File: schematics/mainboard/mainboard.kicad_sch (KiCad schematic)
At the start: 50 parts

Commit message: SCH: maionboard base, routing in progress
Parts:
- removed C10, C11, C12, C13, C14, C15, C16, C17, C18, C19, C5, C6, C7, C8, C9: ~, symbol Arduino_MEGA_2560-Rev3:SMARTPRJ_C-EU0603-RND
- removed D1: ~, symbol Arduino_MEGA_2560-Rev3:DIODE_DIODE-SMB
- removed D2, D3: ~, symbol Arduino_MEGA_2560-Rev3:DIODE_DIODE-MINIMELF
- removed F1: ~, symbol Arduino_MEGA_2560-Rev3:RCL_L-EUL1812
- removed GROUND1, RESET-EN1: ~, symbol Arduino_MEGA_2560-Rev3:JUMPER_SJ
- removed IC1: ~, symbol Arduino_MEGA_2560-Rev3:LINEAR_MC33269ST-3.3T3
- removed IC2: ~, symbol Arduino_MEGA_2560-Rev3:LINEAR_LMV358MMX
- removed IC3: ~, symbol Arduino_MEGA_2560-Rev3:SMARTPRJ_ATMEGA25602560-16AU
- removed IC4: ~, symbol Arduino_MEGA_2560-Rev3:SMARTPRJ_LP2985-XXDBVR33
- removed IC5: ~, symbol Arduino_MEGA_2560-Rev3:SMARTPRJ_ATMEGA16U2-MU
- removed ICSP1_1, ICSP_1: ~, symbol Arduino_MEGA_2560-Rev3:SMARTPRJ_PINHD-2X3
- removed JP3: ~, symbol Arduino_MEGA_2560-Rev3:SMARTPRJ_PINHD-2X2
- removed L2: ~, symbol Arduino_MEGA_2560-Rev3:WUERTH-ELEKTRONIK_WE-CBF_0805
- removed PC1, PC2: ~, symbol Arduino_MEGA_2560-Rev3:RCL_CPOL-EUD
- removed POWER1: ~, symbol Arduino_MEGA_2560-Rev3:SMARTPRJ_PINHD-1X8
- removed R3, R4: ~, symbol Arduino_MEGA_2560-Rev3:SMARTPRJ_R-EU_R0603
- removed RESET1: ~, symbol Arduino_MEGA_2560-Rev3:SMARTPRJ_TS42
- removed RN1, RN4: ~, symbol Arduino_MEGA_2560-Rev3:RESISTOR-DIL_4R-NCAT16
- removed RN2, RN3, RN5: ~, symbol Arduino_MEGA_2560-Rev3:RESISTOR-DIL_4R-NCAY16
- removed RX1, TX1: ~, symbol Arduino_MEGA_2560-Rev3:LED_LEDCHIP-LED0805
- removed T1: ~, symbol Arduino_MEGA_2560-Rev3:ZETEX_PMOSSOT23
- removed X1: ~, symbol Arduino_MEGA_2560-Rev3:SMARTPRJ_POWERSUPPLY_DC21MMX
- removed X2: ~, symbol Arduino_MEGA_2560-Rev3:SMARTPRJ_PN61729
- removed Y1: ~, symbol Arduino_MEGA_2560-Rev3:SMARTPRJ_RESONATORMU
- removed Y2: ~, symbol Arduino_MEGA_2560-Rev3:SMARTPRJ_XTAL_S
- removed Z1, Z2: ~, symbol Arduino_MEGA_2560-Rev3:VARISTOR_VARISTORCN0603
- added C1, C2, C3, C4, C5, C6: 0.1uF, Capacitor_SMD:C_0603_1608Metric, symbol Device:C
- added C7, C8: 22pF, Capacitor_SMD:C_0603_1608Metric, symbol Device:C_Small
- added D1, D2: LED, LED_SMD:LED_1206_3216Metric, symbol Device:LED
- added J1: ICSP, Connector_PinHeader_2.54mm:PinHeader_2x03_P2.54mm_Vertical, symbol Connector_Generic:Conn_02x03_Odd_Even
- added J2: USB_B_Micro, Connector_USB:USB_Micro-B_GCT_USB3076-30-A, symbol Connector:USB_B_Micro
- added J3: Jack-DC, Connector_BarrelJack:BarrelJack_CLIFF_FC681465S_SMT_Horizontal, symbol Connector:Jack-DC
- added J4: PWR_SELECT, Connector_PinHeader_2.54mm:PinHeader_1x03_P2.54mm_Vertical, symbol Connector:Conn_01x03_Pin
- added R1, R2, R4, R5: 1k, Resistor_SMD:R_0603_1608Metric, symbol Device:R
- added R3: 10K, Resistor_SMD:R_0603_1608Metric, symbol Device:R
- added U1: ATmega2560-16A, Package_QFP:TQFP-100_14x14mm_P0.5mm, symbol MCU_Microchip_ATmega:ATmega2560-16A
- added U2: FT232RL, Package_SO:SSOP-28_5.3x10.2mm_P0.65mm, symbol Interface_USB:FT232RL
- added Y1: 16Mhz, Crystal:Crystal_HC52-8mm_Vertical, symbol Device:Crystal
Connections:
- net +5V: now also C1.1, C2.1, C3.1, C4.1, J1.2 (Pin_2), J4.2 (Pin_2), R3.1, R4.2, R5.2, U1.10 (VCC), U1.100 (AVCC), U1.31 (VCC), U1.61 (VCC), U1.80 (VCC), U2.19 (~{RESET}), U2.20 (VCC), U2.4 (VCCIO)
- net DTR: now also C6.2, U2.2 (DTR)
- net GND: now also C1.2, C2.2, C3.2, C4.2, C5.2, C7.2, C8.2, J1.6 (Pin_6), J2.5 (GND), J2.6 (Shield), J3.2, U1.11 (GND), U1.32 (GND), U1.62 (GND), U1.81 (GND), U1.99 (GND), U2.18 (GND), U2.21 (GND), U2.25 (AGND), U2.7 (GND)
- net RESET: now also C5.1, C6.1, J1.5 (Pin_5), R3.2, U1.30 (~{RESET})
- new net: R1.1, U2.1 (TXD)
- new net: R1.2, U1.2 (PE0)
- new net: C7.1, U1.34 (XTAL1), Y1.1
- new net: C8.1, U1.33 (XTAL2), Y1.2
- new net: J2.1 (VBUS), J4.3 (Pin_3)
- new net: J2.2 (D-), U2.16 (USBD-)
- new net: J2.3 (D+), U2.15 (USBD+)
- new net: R2.1, U2.5 (RXD)
- new net: R2.2, U1.3 (PE1)
- new net: J3.1, J4.1 (Pin_1)
- new net: D2.1 (K), U2.22 (CBUS1)
- new net: D2.2 (A), R5.1
- new net: D1.1 (K), U2.23 (CBUS0)
- new net: D1.2 (A), R4.1
- new net MISO: J1.1 (Pin_1), U1.22 (PB3)
- new net MOSI: J1.4 (Pin_4), U1.21 (PB2)
- new net SCK: J1.3 (Pin_3), U1.20 (PB1)
- no-connect marks 81 -> 9
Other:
- note added: "Programming header"
- note removed: "(MISO)"
- note removed: "(MOSI)"
- note removed: "(RX0)"
- note removed: "(SCK)"
- note removed: "(TX0)"
- note removed: "USB boot En"

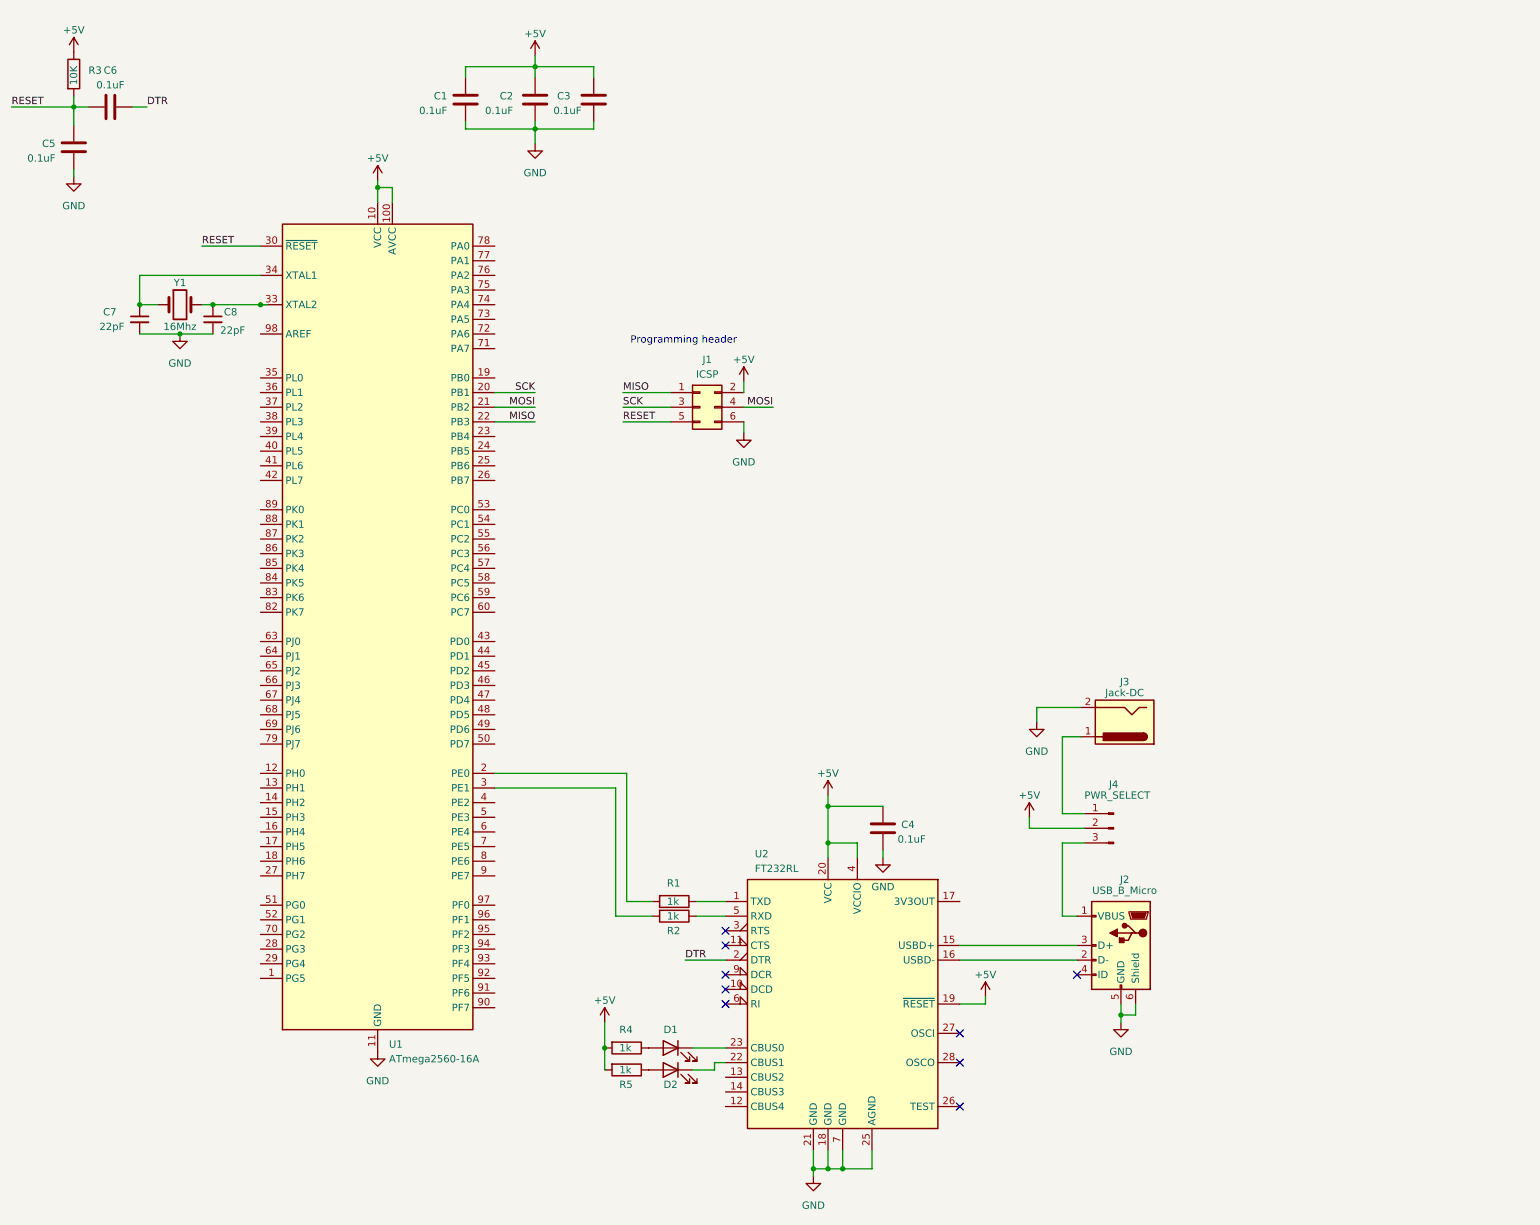
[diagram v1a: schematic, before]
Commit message: SCH: mainboard: cont.
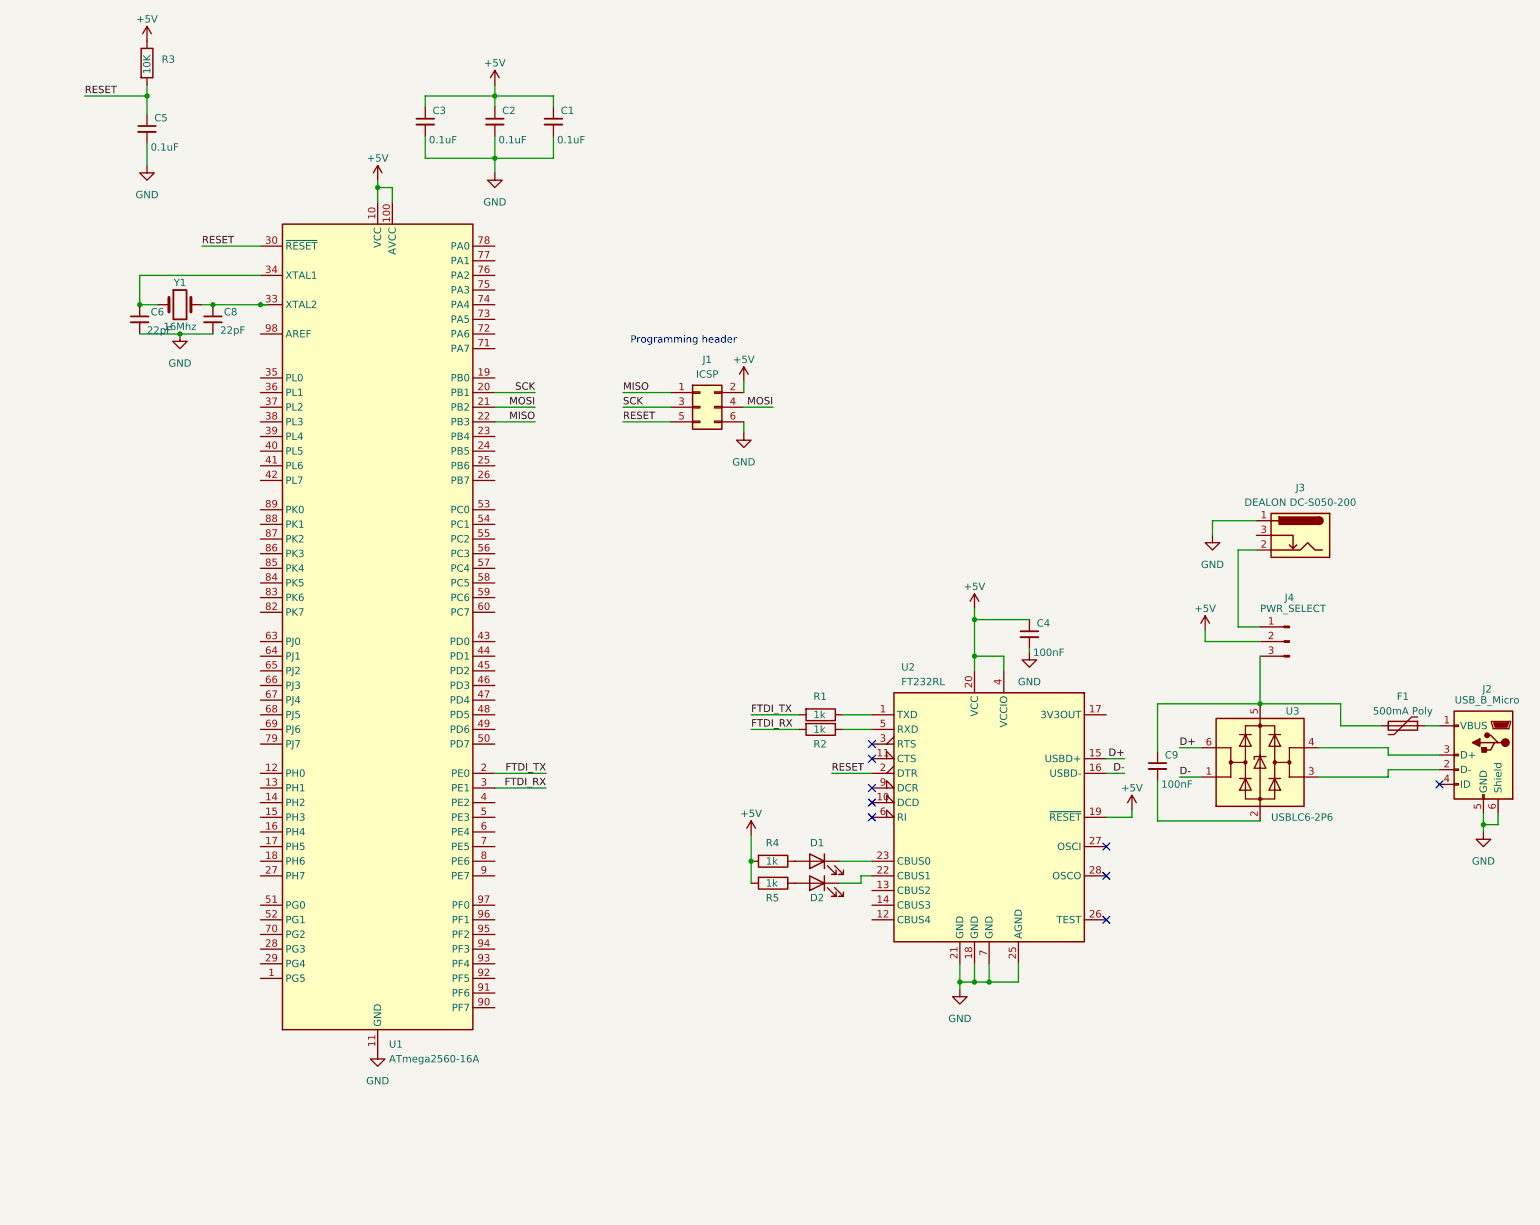
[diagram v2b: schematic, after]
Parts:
- removed C1, C2, C3, C4, C5, C6: 0.1uF, Capacitor_SMD:C_0603_1608Metric, symbol Device:C
- removed C7: 22pF, Capacitor_SMD:C_0603_1608Metric, symbol Device:C_Small
- removed J3: Jack-DC, Connector_BarrelJack:BarrelJack_CLIFF_FC681465S_SMT_Horizontal, symbol Connector:Jack-DC
- added C1, C2, C3, C5: 0.1uF, Capacitor_SMD:C_0201_0603Metric, symbol Device:C_Small
- added C4, C9: 100nF, Capacitor_SMD:C_0201_0603Metric, symbol Device:C_Small
- added C6: 22pF, Capacitor_SMD:C_0603_1608Metric, symbol Device:C_Small
- added F1: 500mA Poly, Fuse:Fuse_0603_1608Metric, symbol Device:Polyfuse
- added J3: DEALON DC-S050-200, Connector_BarrelJack:BarrelJack_CLIFF_FC681465S_SMT_Horizontal, symbol Connector:Barrel_Jack_Switch
- added U3: USBLC6-2P6, Package_TO_SOT_SMD:SOT-666, symbol Power_Protection:USBLC6-2P6
- C8: lcsc (none) -> C105620
- J2: footprint Connector_USB:USB_Micro-B_GCT_USB3076-30-A -> Connector_USB:USB_Micro-B_Molex-105017-0001; lcsc (none) -> C962222
- R1, R2, R4, R5: lcsc (none) -> C21190
- R3: lcsc (none) -> C25804
- U1: lcsc (none) -> C22460
- U2: footprint Package_SO:SSOP-28_5.3x10.2mm_P0.65mm -> Package_DFN_QFN:HVQFN-32-1EP_5x5mm_P0.5mm_EP3.1x3.1mm
- Y1: footprint Crystal:Crystal_HC52-8mm_Vertical -> Crystal:Crystal_SMD_5032-2Pin_5.0x3.2mm; lcsc (none) -> C112572
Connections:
- net DTR is gone; now on net RESET: U2.2 (DTR)
- net +5V: now also C1.1, C2.1, C3.1, C4.1
- net GND: now also C1.2, C2.2, C3.2, C4.2, C5.2, C6.2, J3.1
- net RESET: now also C5.1
- net FTDI_TX: now reaches R1.2, U1.2 (PE0)
- net at U1.34 (XTAL1), Y1.1: now also C6.1
- net at J2.1 (VBUS): now also F1.1; no longer J4.3 (Pin_3)
- net at J2.2 (D-): now also U3.3 (I/O2); no longer U2.16 (USBD-)
- net at J2.3 (D+): now also U3.4 (I/O2); no longer U2.15 (USBD+)
- net FTDI_RX: now reaches R2.2, U1.3 (PE1)
- net at J4.1 (Pin_1): now also J3.2
- new net: C9.1, F1.2, J4.3 (Pin_3), U3.5 (VBUS)
- new net: C9.2, U3.2 (GND)
- new net D+: U2.15 (USBD+), U3.6 (I/O1)
- new net D-: U2.16 (USBD-), U3.1 (I/O1)
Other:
- moved on the sheet: D1, D2, J2, J4, R1, R2, R3, R4, R5, U2

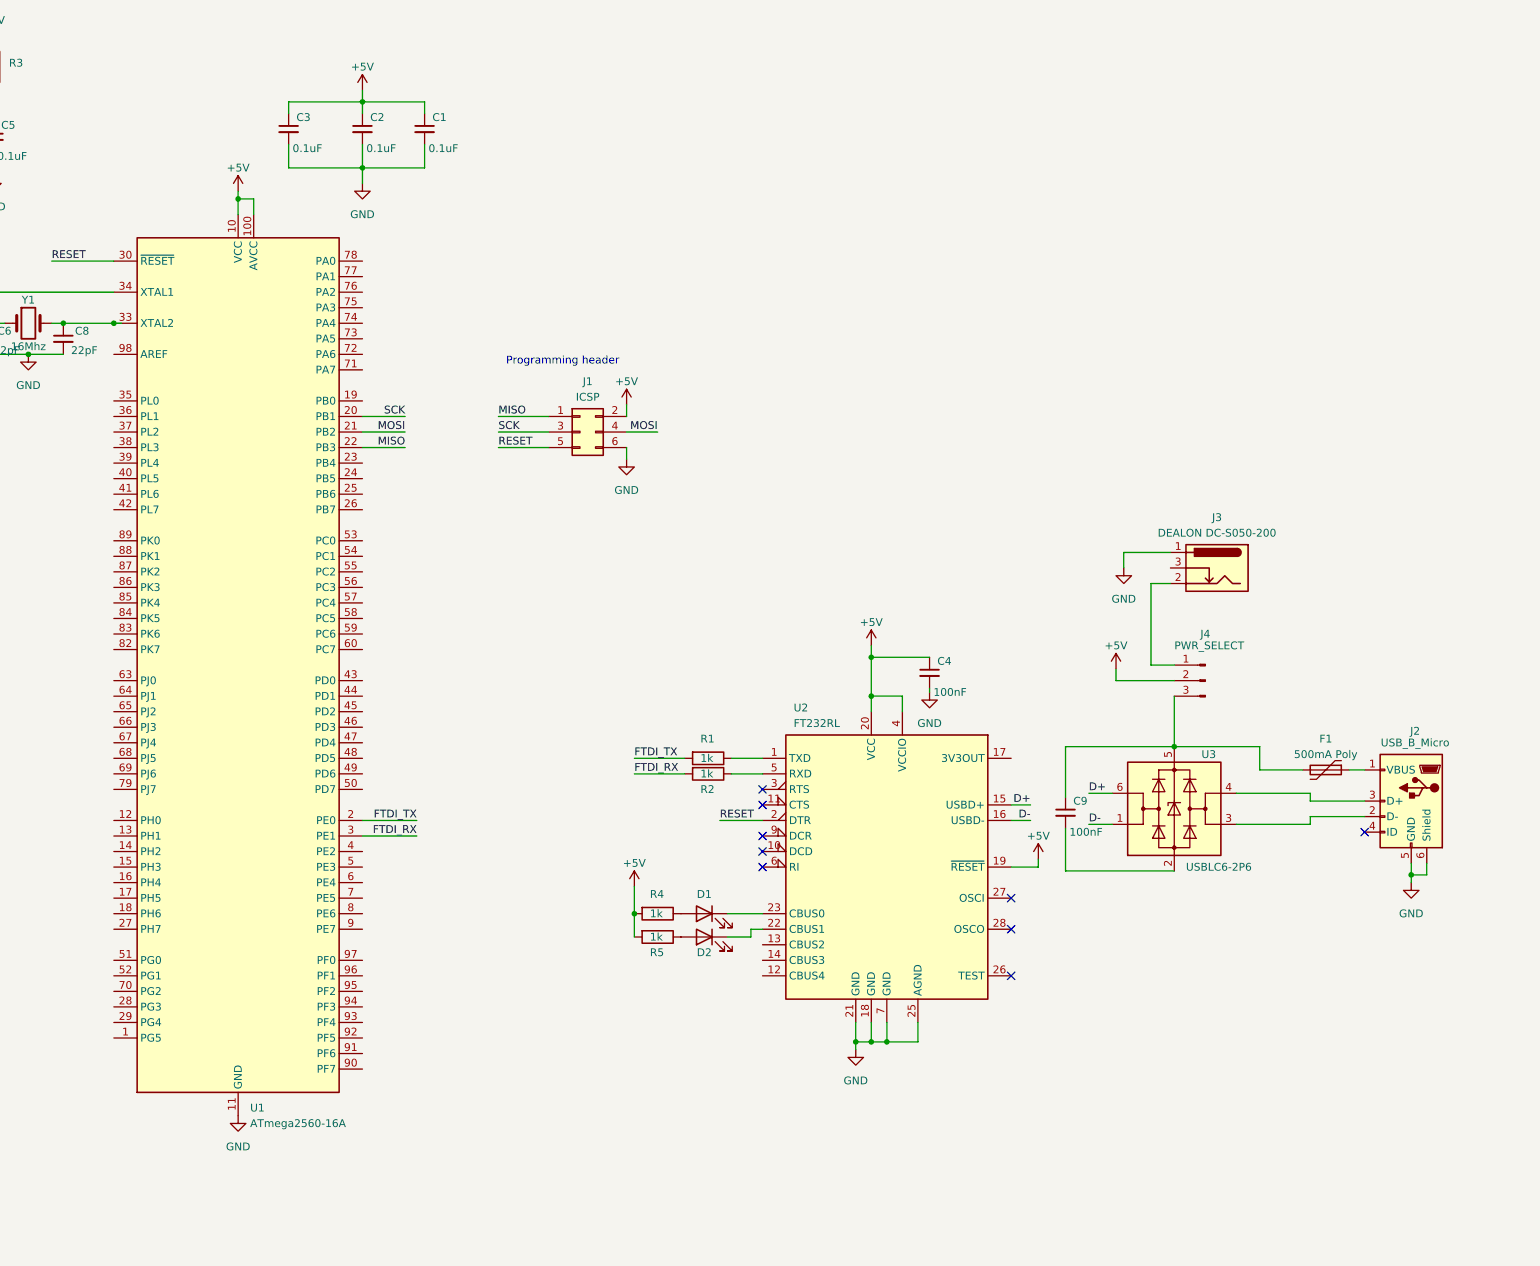
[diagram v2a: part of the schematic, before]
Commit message: SCH: mainboard=> +regu on VIN. routing cont.
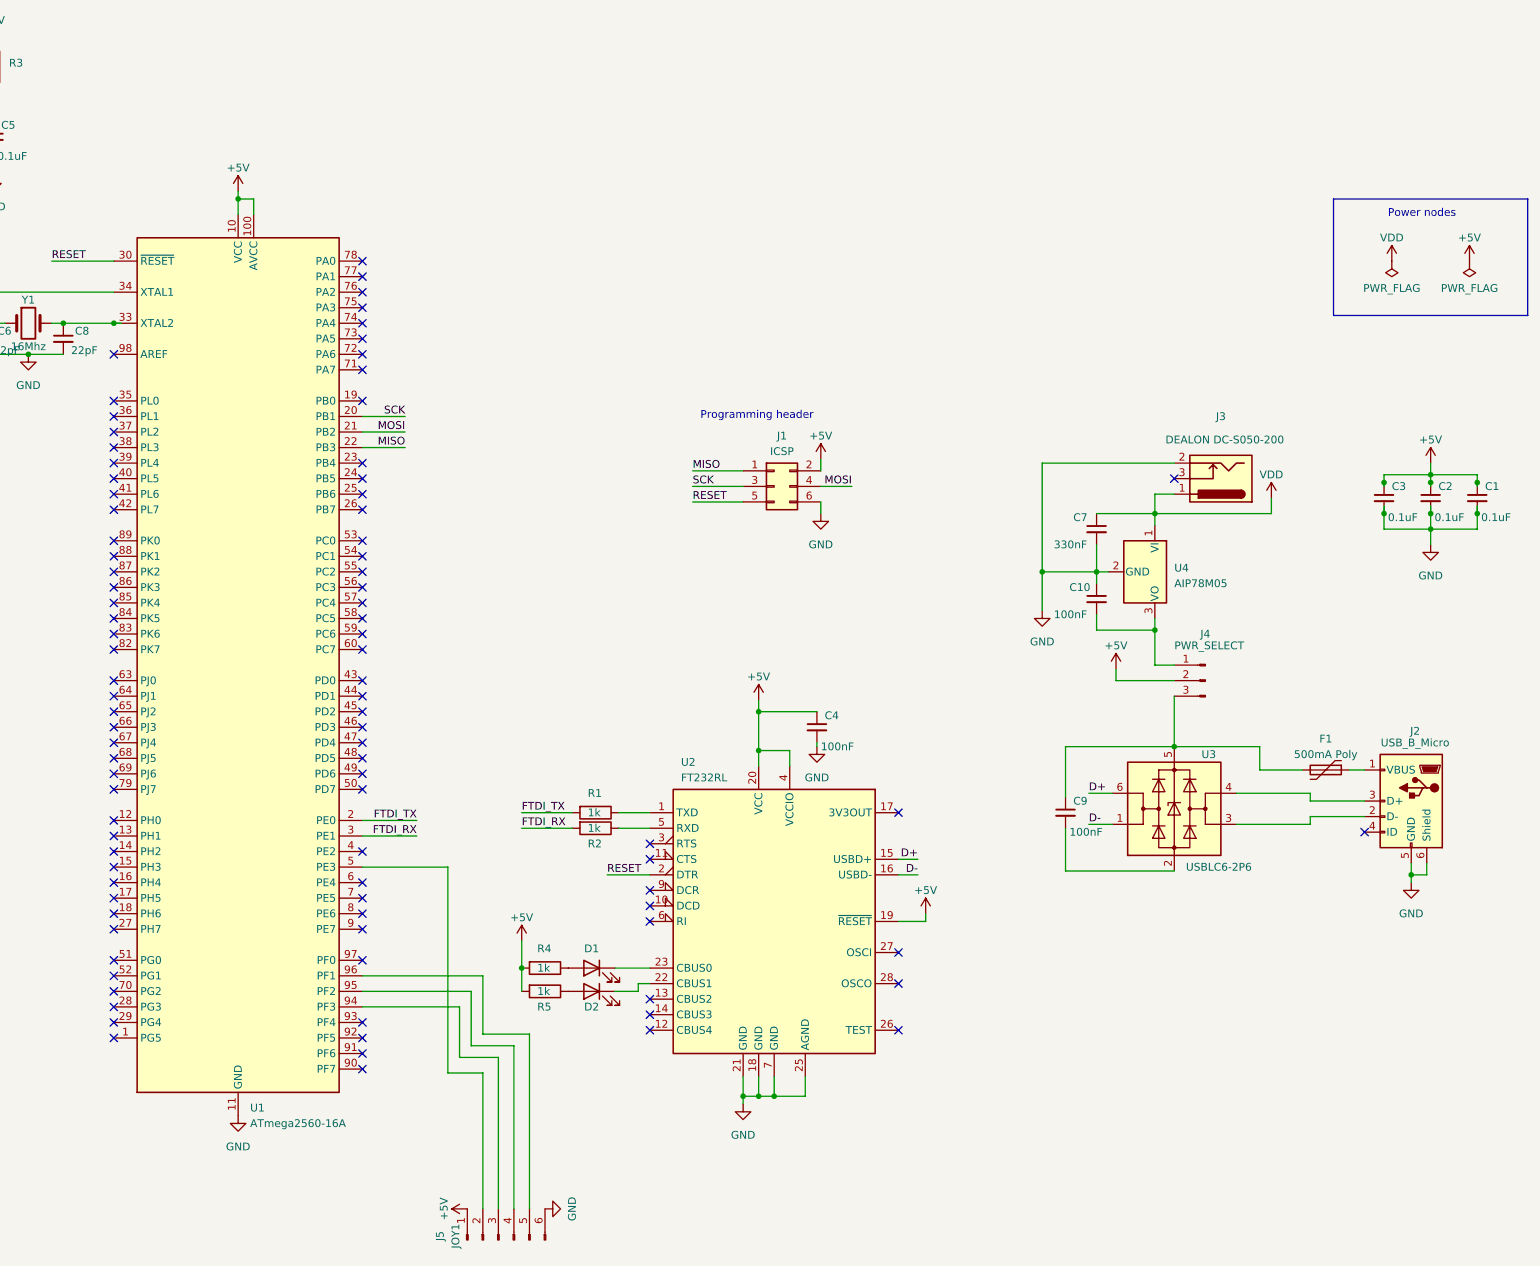
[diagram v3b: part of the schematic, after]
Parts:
- added C10: 100nF, Capacitor_SMD:C_0603_1608Metric, symbol Device:C_Small
- added C7: 330nF, Capacitor_SMD:C_0603_1608Metric, symbol Device:C_Small
- added J5: JOY1, Connector_JST:JST_PH_B6B-PH-K_1x06_P2.00mm_Vertical, symbol Connector:Conn_01x06_Pin
- added U4: AIP78M05, Package_TO_SOT_SMD:TO-252-2, symbol Regulator_Linear:LM78M05_TO252
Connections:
- net +5V: now also J5.1 (Pin_1)
- net GND: now also J3.2, C10.1, C7.2, J5.6 (Pin_6), U4.2 (GND); no longer J3.1
- net at J4.1 (Pin_1): now also C10.2, U4.3 (VO); no longer J3.2
- net at U1.5 (PE3): now also J5.2 (Pin_2)
- net at U1.94 (PF3): now also J5.3 (Pin_3)
- net at U1.95 (PF2): now also J5.4 (Pin_4)
- net at U1.96 (PF1): now also J5.5 (Pin_5)
- new net VDD: C7.1, J3.1, U4.1 (VI)
- no-connect marks 9 -> 92
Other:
- note added: "Power nodes"
- moved on the sheet: C1, C2, C3, C4, D1, D2, J1, J3, R1, R2, R4, R5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
